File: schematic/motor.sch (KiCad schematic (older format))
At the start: 23 parts, among them U2 TMC2130

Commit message: routed 3.3V power and start re arange signals
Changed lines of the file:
@@
 EESchema Schematic File Version 2
+LIBS:74xgxx
+LIBS:74xx
+LIBS:ac-dc
+LIBS:actel
+LIBS:adc-dac
+LIBS:allegro
+LIBS:Altera
+LIBS:analog_devices
+LIBS:analog_switches
+LIBS:atmel
+LIBS:audio
+LIBS:battery_management
+LIBS:bbd
+LIBS:bosch
+LIBS:brooktre
+LIBS:cmos4000
+LIBS:cmos_ieee
+LIBS:conn
+LIBS:contrib
+LIBS:cypress
+LIBS:dc-dc
+LIBS:device
+LIBS:digital-audio
+LIBS:diode
+LIBS:display
+LIBS:dsp
+LIBS:elec-unifil
+LIBS:ESD_Protection
+LIBS:ftdi
+LIBS:gennum
+LIBS:graphic_symbols
+LIBS:hc11
+LIBS:infineon
+LIBS:intel
+LIBS:interface
+LIBS:intersil
+LIBS:ir
+LIBS:Lattice
+LIBS:leds
+LIBS:LEM
+LIBS:linear
+LIBS:logic_programmable
+LIBS:maxim
+LIBS:mechanical
+LIBS:memory
+LIBS:microchip
+LIBS:microchip_dspic33dsc
+LIBS:microchip_pic10mcu
+LIBS:microchip_pic12mcu
+LIBS:microchip_pic16mcu
+LIBS:microchip_pic18mcu
+LIBS:microchip_pic24mcu
+LIBS:microchip_pic32mcu
+LIBS:microcontrollers
+LIBS:modules
+LIBS:motor_drivers
+LIBS:motorola
+LIBS:motors
+LIBS:msp430
+LIBS:nordicsemi
+LIBS:nxp
+LIBS:nxp_armmcu
+LIBS:onsemi
+LIBS:opto
+LIBS:Oscillators
+LIBS:philips
 LIBS:power
-LIBS:device
+LIBS:powerint
+LIBS:Power_Management
+LIBS:pspice
+LIBS:references
+LIBS:regul
+LIBS:relays
+LIBS:rfcom
+LIBS:RFSolutions
+LIBS:sensors
+LIBS:silabs
+LIBS:siliconi
+LIBS:stm8
+LIBS:stm32
+LIBS:supertex
 LIBS:switches
-LIBS:relays
-LIBS:motors
+LIBS:texas
+LIBS:transf
 LIBS:transistors
-LIBS:conn
-LIBS:linear
-LIBS:regul
-LIBS:74xx
-LIBS:cmos4000
-LIBS:adc-dac
-LIBS:memory
+LIBS:triac_thyristor
+LIBS:ttl_ieee
+LIBS:valves
+LIBS:video
+LIBS:wiznet
+LIBS:Worldsemi
+LIBS:Xicor
 LIBS:xilinx
-LIBS:microcontrollers
-LIBS:dsp
-LIBS:microchip
-LIBS:analog_switches
-LIBS:motorola
-LIBS:texas
-LIBS:intel
-LIBS:audio
-LIBS:interface
-LIBS:digital-audio
-LIBS:philips
-LIBS:display
-LIBS:cypress
-LIBS:siliconi
-LIBS:opto
-LIBS:atmel
-LIBS:contrib
-LIBS:valves
+LIBS:zetex
+LIBS:Zilog
+LIBS:bd9e302efj
+LIBS:psmn1
 LIBS:tmc2130
+LIBS:schematic-cache
 EELAYER 25 0
 EELAYER END
 $Descr A4 11693 8268
 encoding utf-8
-Sheet 1 1
+Sheet 1 10
 Title ""
 Date ""
@@
 	4050 3300 4300 3300
 Wire Wire Line
-	4600 5150 4700 5150
-Wire Wire Line
-	4700 5150 4800 5150
-Wire Wire Line
-	4800 5150 4950 5150
-Wire Wire Line
-	4950 5150 5150 5150
-Wire Wire Line
-	5150 5150 5700 5150
-Wire Wire Line
-	5700 5150 5800 5150
+	4600 5150 5800 5150
 Connection ~ 5700 5150
 Wire Wire Line
-	3400 4050 3700 4050
-Wire Wire Line
-	3700 4050 4300 4050
+	3400 4050 4300 4050
 Wire Wire Line
 	4300 3700 4050 3700
 Wire Wire Line
-	3400 3950 3550 3950
-Wire Wire Line
-	3550 3950 4300 3950
+	3400 3950 4300 3950
 Wire Wire Line
 	3550 3800 3550 3950
@@
 	4300 4500 4200 4500
 Wire Wire Line
-	4200 4500 4200 4650
-Wire Wire Line
-	4200 4650 4200 4800
+	4200 4500 4200 4800
 Wire Wire Line
 	4600 5150 4600 5300
@@
 	5550 2250 5550 2350
 Wire Wire Line
-	5400 1950 5550 1950
-Wire Wire Line
-	5550 1950 5800 1950
-Wire Wire Line
-	5800 1950 6050 1950
+	5400 1950 6050 1950
 Wire Wire Line
 	5800 1950 5800 2350
@@
 	4000 2700 4000 2800
 Wire Wire Line
-	4000 2800 4200 2800
-Wire Wire Line
-	4200 2800 4300 2800
+	4000 2800 4300 2800
 Wire Wire Line
 	4200 2700 4200 2800
@@
 Connection ~ 5550 1950
 Wire Wire Line
-	5250 1700 5250 1750
-Wire Wire Line
-	5250 1750 5250 2350
+	5250 1700 5250 2350
 Wire Wire Line
 	5700 1750 5800 1750
@@
 	6250 2150 6250 2050
 Wire Wire Line
-	6250 2050 6550 2050
-Wire Wire Line
-	6550 2050 6850 2050
+	6250 2050 6850 2050
 Connection ~ 6550 2050
 Wire Wire Line
-	6250 1750 6550 1750
-Wire Wire Line
-	6550 1750 6850 1750
+	6250 1750 6850 1750
 Connection ~ 6550 1750
 Wire Wire Line
@@
 Connection ~ 6250 2050
 Wire Wire Line
-	6100 2800 7450 2800
-Wire Wire Line
-	7450 2800 7500 2800
-Wire Wire Line
-	6100 3000 7450 3000
-Wire Wire Line
-	7450 3000 7500 3000
-Wire Wire Line
-	7800 2800 7800 2900
-Wire Wire Line
-	7800 2900 7800 3000
+	6100 2800 7500 2800
+Wire Wire Line
+	6100 3000 7500 3000
+Wire Wire Line
+	7800 2800 7800 3000
 Wire Wire Line
 	8150 2600 7450 2600
@@
 	6200 2900 6100 2900
 Wire Wire Line
-	6200 2400 6200 2650
-Wire Wire Line
-	6200 2650 6200 2900
-Wire Wire Line
-	6500 2400 6500 2550
-Wire Wire Line
-	6500 2550 6500 2650
+	6200 2400 6200 2900
+Wire Wire Line
+	6500 2400 6500 2650
 Wire Wire Line
 	6650 2550 6500 2550
@@
 $EndComp
 Wire Wire Line
-	6200 3350 6200 3600
-Wire Wire Line
-	6200 3600 6200 3850
-Wire Wire Line
-	6500 3600 6500 3700
-Wire Wire Line
-	6500 3700 6500 3850
+	6200 3350 6200 3850
+Wire Wire Line
+	6500 3600 6500 3850
 Wire Wire Line
 	6650 3700 6500 3700
@@
 $EndComp
 Wire Wire Line
-	6100 3450 7450 3450
-Wire Wire Line
-	7450 3450 7500 3450
-Wire Wire Line
-	6100 3250 7450 3250
-Wire Wire Line
-	7450 3250 7500 3250
-Wire Wire Line
-	7800 3250 7800 3350
-Wire Wire Line
-	7800 3350 7800 3450
+	6100 3450 7500 3450
+Wire Wire Line
+	6100 3250 7500 3250
+Wire Wire Line
+	7800 3250 7800 3450
 Wire Wire Line
 	8150 3650 7450 3650

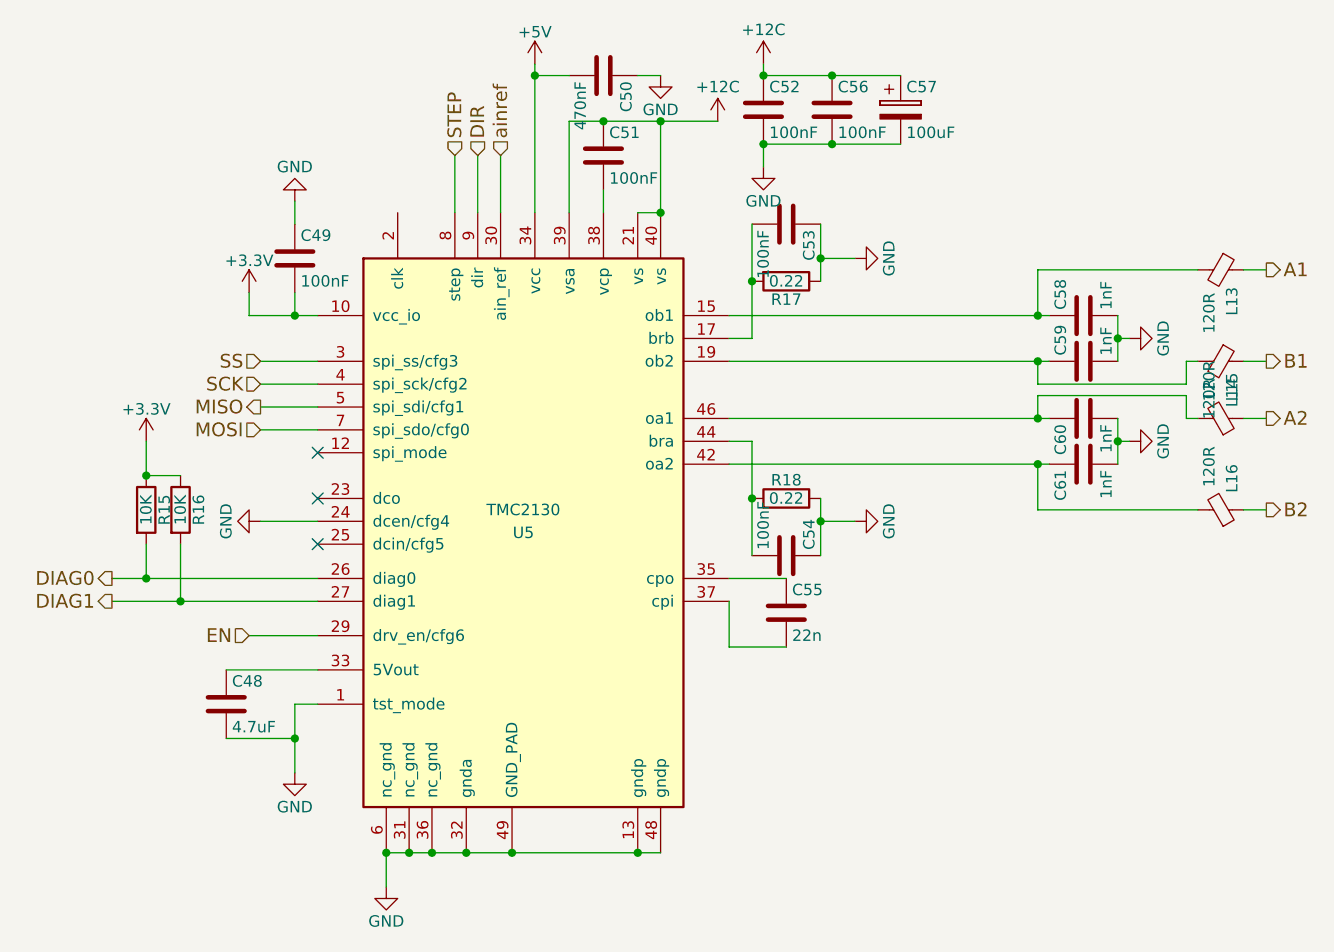
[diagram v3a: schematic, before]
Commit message: Changed footprint size of some capacitors
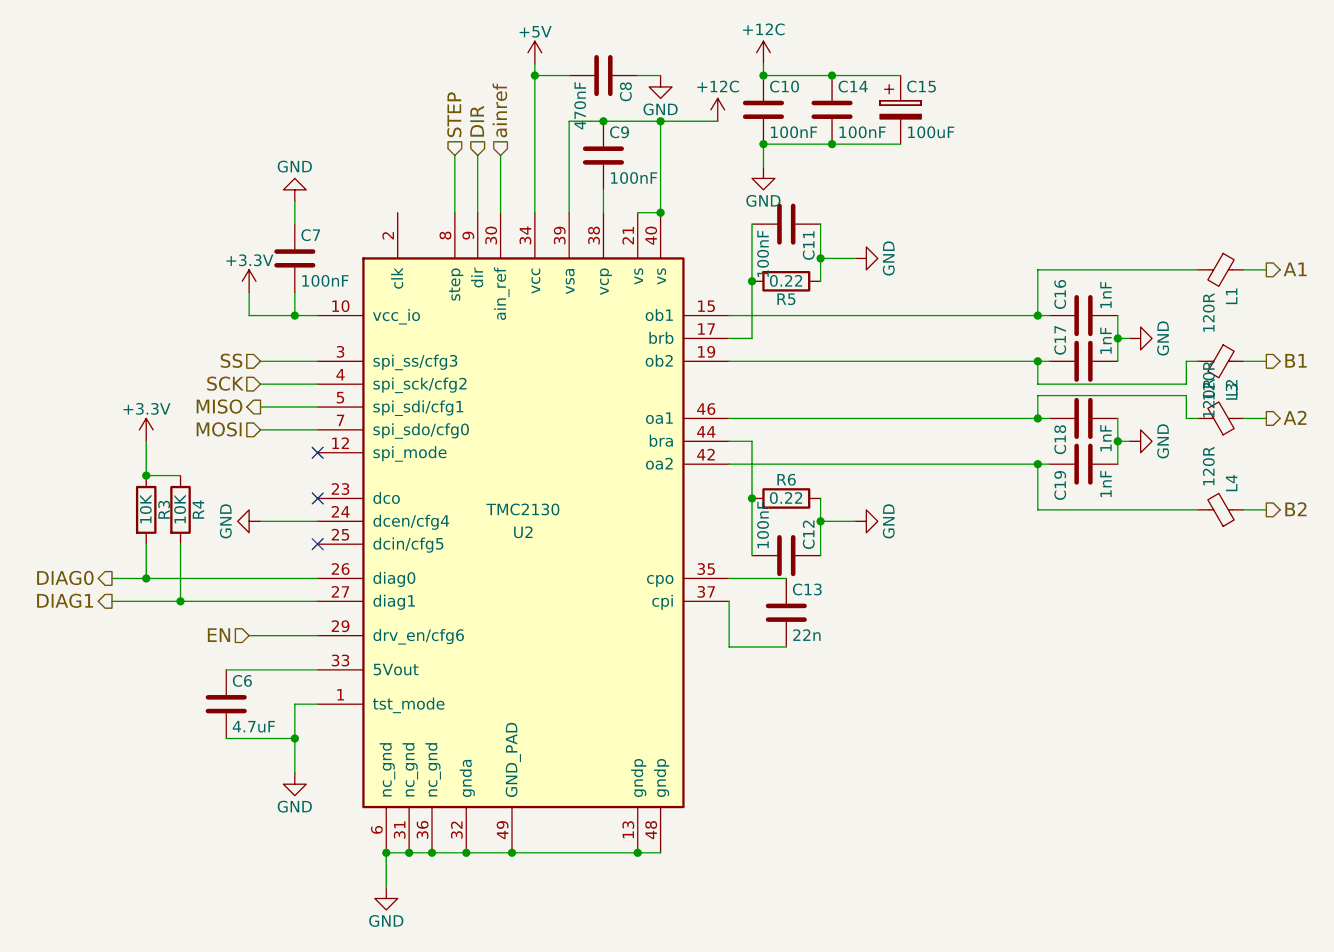
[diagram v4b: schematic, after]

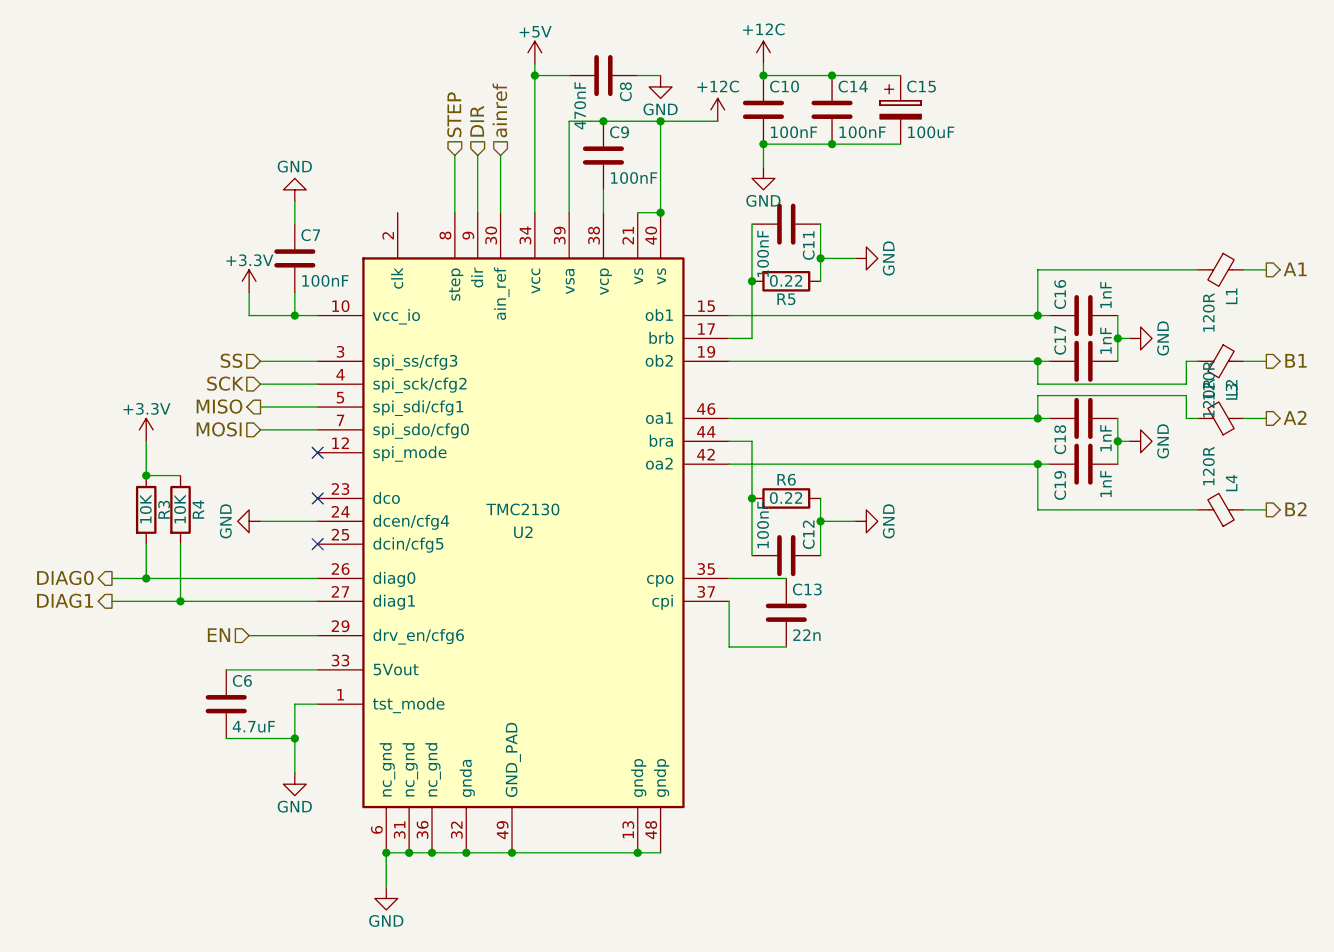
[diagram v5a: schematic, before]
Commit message: Switch orange pi to raspberry pi zero w because the price difference is small
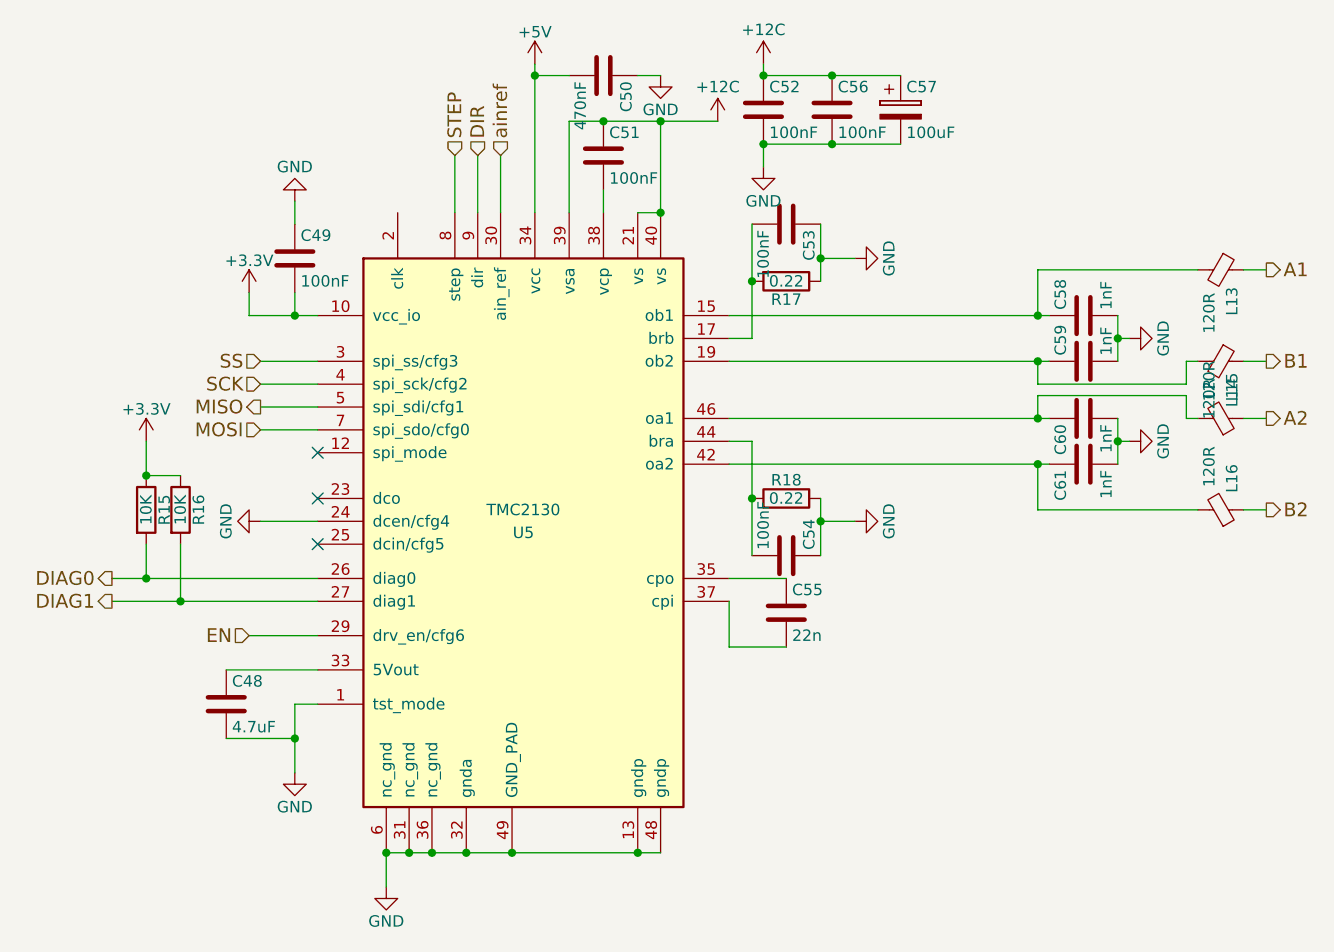
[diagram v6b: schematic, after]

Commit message: Updated to kicad 5.0.0
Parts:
- C10, C11, C12, C13, C14, C16, C17, C18, C19, C6, C7, C8, C9: symbol C -> Device:C
- C15: symbol CP -> Device:CP
- L1, L2, L3, L4: symbol Ferrite_Bead_Small -> Device:Ferrite_Bead_Small
- R3, R4, R5, R6: symbol R -> Device:R
- U2: symbol TMC2130 -> tmc2130:TMC2130

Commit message: Revert "Updated to kicad 5.0.0"
This reverts commit 6c14fa6c8e6361c9b9ee4065803a5a63755fc6a7.
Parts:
- C10, C11, C12, C13, C14, C16, C17, C18, C19, C6, C7, C8, C9: symbol Device:C -> C
- C15: symbol Device:CP -> CP
- L1, L2, L3, L4: symbol Device:Ferrite_Bead_Small -> Ferrite_Bead_Small
- R3, R4, R5, R6: symbol Device:R -> R
- U2: symbol tmc2130:TMC2130 -> TMC2130
